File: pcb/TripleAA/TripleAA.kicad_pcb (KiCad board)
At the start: 2 copper layers, 16 x 20 mm, 12 parts, among them J2 JST_S2B-PH-SM4-x, U2 TPS562242

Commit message: Update SCH and PCB
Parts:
- added C1: 10uF,25V,X5R,0603, Capacitor_SMD:C_0603_1608Metric_Pad1.08x0.95mm_HandSolder, F.Cu at (98.6, 61.6)
- added C2: 10uF,25V,X5R,0603, Capacitor_SMD:C_0603_1608Metric_Pad1.08x0.95mm_HandSolder, F.Cu at (92.9, 61.6)
- added D1: 824021, Package_TO_SOT_SMD_User:SOT-23_Handsoldering, F.Cu at (101.3, 60.0)
- added D2: 150080GS75000, LED_SMD:LED_0805_2012Metric_Pad1.15x1.40mm_HandSolder, F.Cu at (92.5, 50.2)
- added D3: 150080SS75000, LED_SMD:LED_0805_2012Metric_Pad1.15x1.40mm_HandSolder, F.Cu at (92.1, 81.0)
- added J1: JST_S2B-PH-SM4-x, Connector_User:JST_PH_S2B-PH-SM4-TB_1x02-1MP_P2.00mm_Horizontal, F.Cu at (98.8, 53.1)
- added R1: 2k,0603, Resistor_SMD:R_0603_1608Metric_Pad0.98x0.95mm_HandSolder, F.Cu at (92.5, 54.1)
- added R2: 2k,0603, Resistor_SMD:R_0603_1608Metric_Pad0.98x0.95mm_HandSolder, F.Cu at (95.8, 59.1)
- added R5: 27.4k,0603, Resistor_SMD:R_0603_1608Metric_Pad0.98x0.95mm_HandSolder, F.Cu at (91.8, 77.7)
- added R6: 10k,0603, Resistor_SMD:R_0603_1608Metric_Pad0.98x0.95mm_HandSolder, F.Cu at (101.3, 65.3)
- added U1: MCP73831-2-OT, Package_TO_SOT_SMD:SOT-23-5, F.Cu at (95.8, 61.6)
- added U3: BD4836G-xx, Package_TO_SOT_SMD:SOT-23-5, F.Cu at (91.8, 74.5)
- L1: value 74438357068 -> 74438356056; footprint Inductor_SMD_User:L_Wurth_WE-MAPI-4030 -> Inductor_SMD_User:L_Wurth_WE-MAPI-4020
- moved J2 27.9 mm to (98.8, 77.9), turned to 0 degrees
- moved C8 13.8 mm to (96.7, 70.9), turned to 90 degrees
- moved C9 10.2 mm to (98.7, 70.9), turned to 90 degrees
- moved R4 10.1 mm to (99.8, 65.3), turned to 90 degrees
- moved R3 8.16 mm to (102.7, 71.0), turned to 90 degrees
- moved C7 8.12 mm to (101.2, 71.0), turned to 90 degrees
- moved U2 7.27 mm to (97.1, 67.8)
- moved C6 7.14 mm to (100.2, 68.2)
- moved C4 6.89 mm to (94.9, 65.7), turned to 90 degrees
- moved L1 6.60 mm to (93.3, 69.7), turned to 180 degrees
- moved C3 4.52 mm to (93.4, 65.7), turned to 90 degrees
- moved C5 4.19 mm to (97.3, 65.7)
- renumbered C2 to C4, C7 to C5, C5 to C6, C6 to C7, C1 to C8, C4 to C9, R1 to R3, R2 to R4
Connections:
- U2 pad 5: +BATT -> Net-(U2-EN)
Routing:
- net /-Vout: track 0.00 -> 14.0 mm
- net Net-(U2-SW): track 0.00 -> 13.4 mm, vias 0 -> 2
- net +BATT: track 0.00 -> 10.9 mm, vias 0 -> 1
- net Net-(U2-EN): track 0.00 -> 4.11 mm
- net Net-(U2-FB): track 0.00 -> 3.84 mm
- net Net-(U2-BST): track 0.00 -> 1.53 mm
- added copper zone on F.Cu, net +BATT
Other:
- board size 16 x 20 mm -> 13.5 x 35 mm

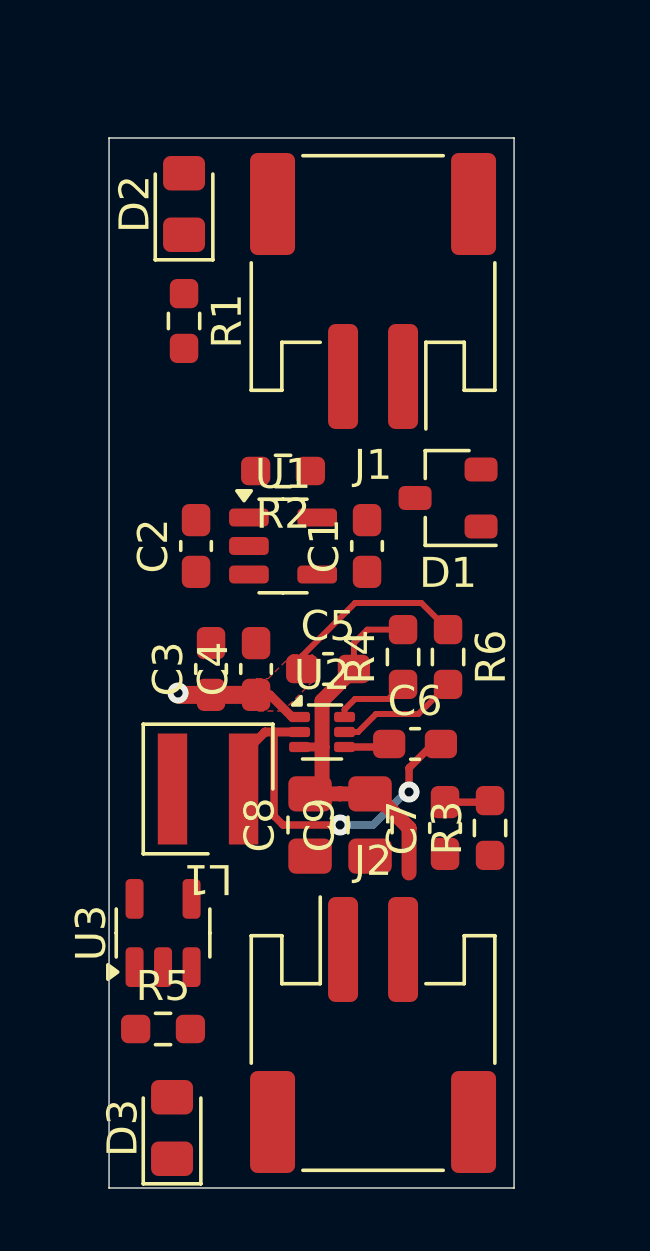
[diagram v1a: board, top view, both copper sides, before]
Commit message: Finalize PCB layout
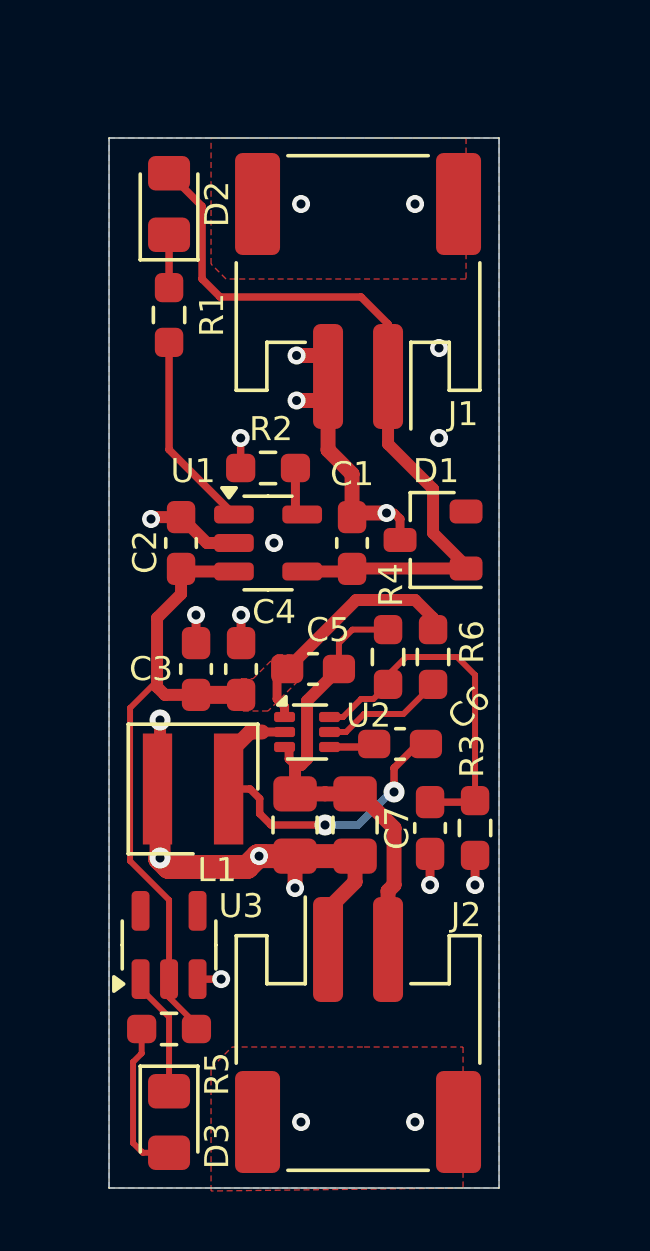
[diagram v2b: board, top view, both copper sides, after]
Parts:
- moved D1 1.49 mm to (100.8, 61.4)
- moved R1 0.54 mm to (92.0, 53.9)
- moved C1 0.51 mm to (98.1, 61.5)
- moved C2 0.51 mm to (92.4, 61.5)
- moved R2 0.51 mm to (95.3, 59.0)
- moved U1 0.51 mm to (95.3, 61.5)
- moved C3 0.50 mm to (92.9, 65.7)
- moved C4 0.50 mm to (94.4, 65.7)
- moved C5 0.50 mm to (96.8, 65.7)
- moved C6 0.50 mm to (99.7, 68.2)
- moved C7 0.50 mm to (100.7, 71.0)
- moved C8 0.50 mm to (96.2, 70.9)
- moved C9 0.50 mm to (98.2, 70.9)
- moved D2 0.50 mm to (92.0, 50.2)
- moved J1 0.50 mm to (98.3, 53.1)
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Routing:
- net GND: track 0.00 -> 35.9 mm, vias 0 -> 21
- net /Vin: track 0.00 -> 25.5 mm
- net +BATT: track 10.9 -> 30.3 mm, vias 1 -> 0
- net Net-(U2-FB): track 3.84 -> 11.6 mm
- net Net-(U1-STAT): track 0.00 -> 6.63 mm
- net Net-(D3-A): track 0.00 -> 5.25 mm
- net Net-(D3-K): track 0.00 -> 4.13 mm
- net /-Vout: track 14.0 -> 17.3 mm
- net Net-(D2-K): track 0.00 -> 1.76 mm
- net Net-(U1-PROG): track 0.00 -> 1.64 mm
- net Net-(U2-SW): track 13.4 -> 12.3 mm
- added copper zone on B.Cu, net GND
- added copper zone on F.Cu, net GND
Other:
- board size 13.5 x 35 mm -> 13 x 35 mm
- board text added: "(+) Vin"
- board text added: "(-) GND"
- board text added: "-Vout (-)"
- board text added: "GND (+)"

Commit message: Add USB connector
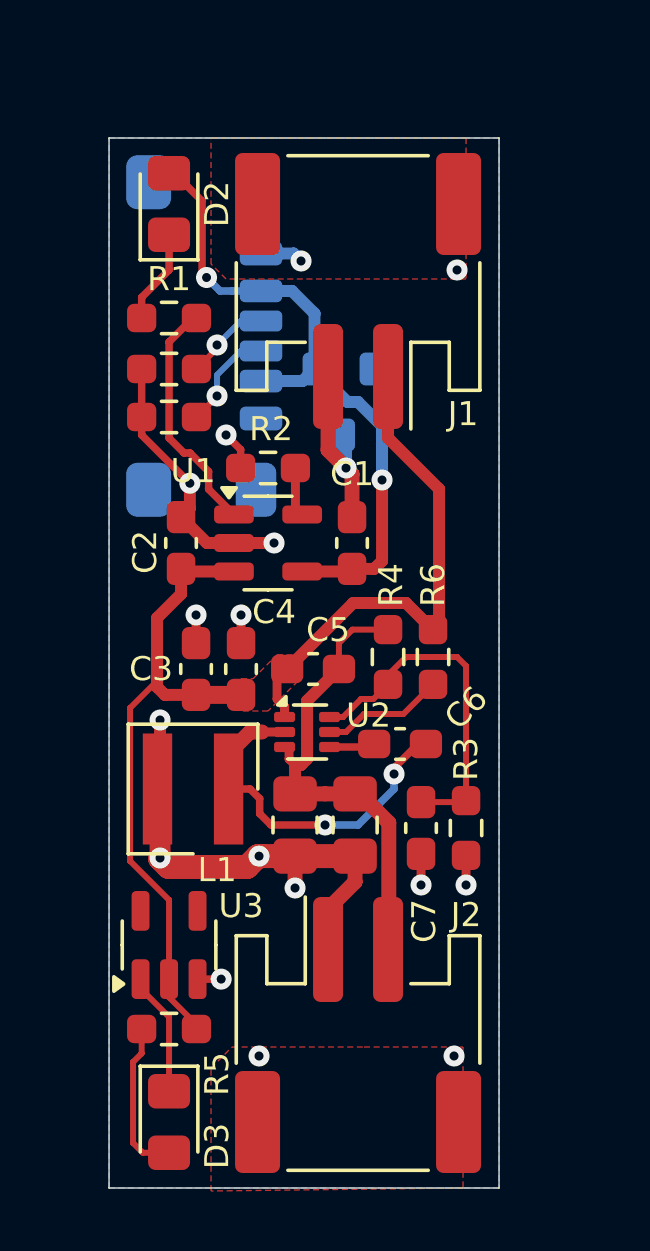
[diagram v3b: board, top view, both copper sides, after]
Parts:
- added J3: USB4135-GF-A, Connector_User:USB-C_Receptacle_GTC_USB4135-GF-A, B.Cu at (94.9, 54.6)
- added R7: 5.1k,0603, Resistor_SMD:R_0603_1608Metric_Pad0.98x0.95mm_HandSolder, F.Cu at (92.0, 55.7)
- added R8: 5.1k,0603, Resistor_SMD:R_0603_1608Metric_Pad0.98x0.95mm_HandSolder, F.Cu at (92.0, 57.3)
- D1: moved to B.Cu
- moved D1 5.49 mm to (97.8, 56.8), turned to -90 degrees
- moved C7 0.30 mm to (100.4, 71.0)
- moved R3 0.30 mm to (101.9, 71.0)
- moved R1 0.10 mm to (92.0, 54.0), turned to 0 degrees
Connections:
- C1 pad 1: /Vin -> /VBUS
- D1 pad 1: /Vin -> /VBUS
- D2 pad 2: /Vin -> /VBUS
- J1 pad 1: /Vin -> +BATT
- U1 pad 4: /Vin -> /VBUS
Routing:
- net /Vin: track 25.5 -> 0.00 mm
- net /VBUS: track 0.00 -> 22.4 mm, vias 0 -> 2
- net +BATT: track 30.3 -> 39.2 mm
- net Net-(J3-CC1): track 0.00 -> 3.48 mm, vias 0 -> 1
- net GND: track 35.9 -> 39.0 mm, vias 21 -> 17
- net Net-(J3-CC2): track 0.00 -> 2.88 mm, vias 0 -> 1
- net Net-(D2-K): track 1.76 -> 3.15 mm
- net Net-(U1-STAT): track 6.63 -> 8.01 mm
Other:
- board text added: "+BATT"
- board text added: "-Vout"
- board text added: "GND"
- board text added: "USB Charge"
- board text removed: "(+) Vin"
- board text removed: "(-) GND"
- board text removed: "-Vout (-)"
- board text removed: "GND (+)"

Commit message: RevA
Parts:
- L1: value 74438356056 -> SRN4018-4R7M; footprint Inductor_SMD_User:L_Wurth_WE-MAPI-4020 -> Inductor_SMD:L_Bourns-SRN4018
- moved D1 1.87 mm to (99.6, 57.3), turned to 180 degrees
- moved J3 1.60 mm to (96.5, 54.6)
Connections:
- D1 pad 2: unconnected-(D1-K-Pad2) -> /VBUS
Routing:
- net /VBUS: track 22.4 -> 25.5 mm
- net GND: track 39.0 -> 35.9 mm
- net Net-(J3-CC2): track 2.88 -> 5.08 mm
- net Net-(J3-CC1): track 3.48 -> 4.66 mm
- net +BATT: track 39.2 -> 40.0 mm, vias 0 -> 2
- net Net-(U2-SW): track 12.3 -> 11.7 mm
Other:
- board text added: "AA BatteryReplacement Rev. A by fl0m0"
